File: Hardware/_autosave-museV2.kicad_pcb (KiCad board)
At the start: 2 copper layers, 288 parts, among them P1 RCA_conn_x2, P10 -15V, P11 ~3, P13 ~4, P14 +5V, P18 RX1, P19 3.3V, P2 +12V, P20 TX2, P21 1.8V, P22 PSU_CTL, P23 GND, P27 D1, P29 D2, P3 3.5mm_conn_tip_switch, P30 D3, P31 P1, P32 L1.8_1, P33 L3.3_1, P34 P2, P35 L1.8_2, P36 L3.3_2, P37 P3, P38 L1.8_3, P39 L3.3_3, P4 3.5mm_conn_tip_switch, P40 P4, P41 L1.8_4, P42 L3.3_4, P43 +5V, P44 +12V_AUX, P45 +5V_AUX, P5 CONN_01X06, P6 CONN_02X14, P7 ~5, P8 +15V, P9 ~6, Q1 PMOS, Q2 BSS138, SW1 PWR_BTN, SW2 PWR_BTN, U1 TPS65130, U10 PCM1863, U11 PCM1796, U12 NE5534, U13 NE5534, U14 NE5534, U15 NE5534, U16 NE5534, U17 NE5534, U18 EdisonConnector, U19 GTL2010, U2 LP38692, U20 GTL2010, U21 GTL2010, U22 PCA9685BS, U3 PLR135/T10, U4 POM-3535L-3-R, U5 POM-3535L-3-R, U6 PLT133/T10W, U7 POM-3535L-3-R, U8 POM-3535L-3-R, U9 PCM9211, X1 24.576 MHz

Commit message: PCB Layout progress - placing PCM9211 components
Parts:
- moved C18 165.2 mm to (184.2, 170.1), turned to 0 degrees
- moved C17 135.9 mm to (185.3, 171.8), turned to 0 degrees
- moved U11 13.4 mm to (166.2, 166.7)
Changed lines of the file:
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@@
   )
   (module Capacitors_SMD:C_0402 (layer F.Cu)
-    (at 29.217212 112.79591 180)
+    (at 184.2 170.05)
     (descr "Capacitor SMD 0402, reflow soldering, AVX (see smccp.pdf)")
     (tags "capacitor 0402")
     (attr smd)
-    (fp_text reference C18 (at 0 -1.7 180) (layer F.SilkS)
+    (fp_text reference C18 (at 0 -1.7) (layer F.SilkS) hide
       (effects (font (size 1 1) (thickness 0.15)))
     )
-    (fp_text value 0.1uF (at 0 1.7 180) (layer F.Fab)
+    (fp_text value 0.1uF (at 0 1.7) (layer F.Fab)
       (effects (font (size 1 1) (thickness 0.15)))
     )
@@
     (fp_line (start 0.25 -0.475) (end -0.25 -0.475) (layer F.SilkS) (width 0.15))
     (fp_line (start -0.25 0.475) (end 0.25 0.475) (layer F.SilkS) (width 0.15))
-    (pad 1 smd rect (at -0.55 0 180) (size 0.6 0.5) (layers F.Cu F.Paste F.Mask)
+    (pad 1 smd rect (at -0.55 0) (size 0.6 0.5) (layers F.Cu F.Paste F.Mask)
       (net 12 +3.3VSB))
-    (pad 2 smd rect (at 0.55 0 180) (size 0.6 0.5) (layers F.Cu F.Paste F.Mask)
+    (pad 2 smd rect (at 0.55 0) (size 0.6 0.5) (layers F.Cu F.Paste F.Mask)
       (net 2 GND))
     (model Capacitors_SMD.3dshapes/C_0402.wrl
@@
   )
   (module Housings_SSOP:SSOP-28_5.3x10.2mm_Pitch0.65mm (layer F.Cu)
-    (at 163.4 153.5 180)
+    (at 166.15 166.65 180)
     (descr "28-Lead Plastic Shrink Small Outline (SS)-5.30 mm Body [SSOP] (see Microchip Packaging Specification 00000049BS.pdf)")
     (tags "SSOP 0.65")
@@
   )
   (module Capacitors_SMD:C_1206 (layer F.Cu)
-    (at 58.473639 122.97091 180)
+    (at 185.3 171.8)
     (descr "Capacitor SMD 1206, reflow soldering, AVX (see smccp.pdf)")
     (tags "capacitor 1206")
     (attr smd)
-    (fp_text reference C17 (at 0 -2.3 180) (layer F.SilkS)
+    (fp_text reference C17 (at 0 -2.3) (layer F.SilkS) hide
       (effects (font (size 1 1) (thickness 0.15)))
     )
-    (fp_text value 10uF (at 0 2.3 180) (layer F.Fab)
+    (fp_text value 10uF (at 0 2.3) (layer F.Fab)
       (effects (font (size 1 1) (thickness 0.15)))
     )
@@
     (fp_line (start 1 -1.025) (end -1 -1.025) (layer F.SilkS) (width 0.15))
     (fp_line (start -1 1.025) (end 1 1.025) (layer F.SilkS) (width 0.15))
-    (pad 1 smd rect (at -1.5 0 180) (size 1 1.6) (layers F.Cu F.Paste F.Mask)
+    (pad 1 smd rect (at -1.5 0) (size 1 1.6) (layers F.Cu F.Paste F.Mask)
       (net 12 +3.3VSB))
-    (pad 2 smd rect (at 1.5 0 180) (size 1 1.6) (layers F.Cu F.Paste F.Mask)
+    (pad 2 smd rect (at 1.5 0) (size 1 1.6) (layers F.Cu F.Paste F.Mask)
       (net 2 GND))
     (model Capacitors_SMD.3dshapes/C_1206.wrl

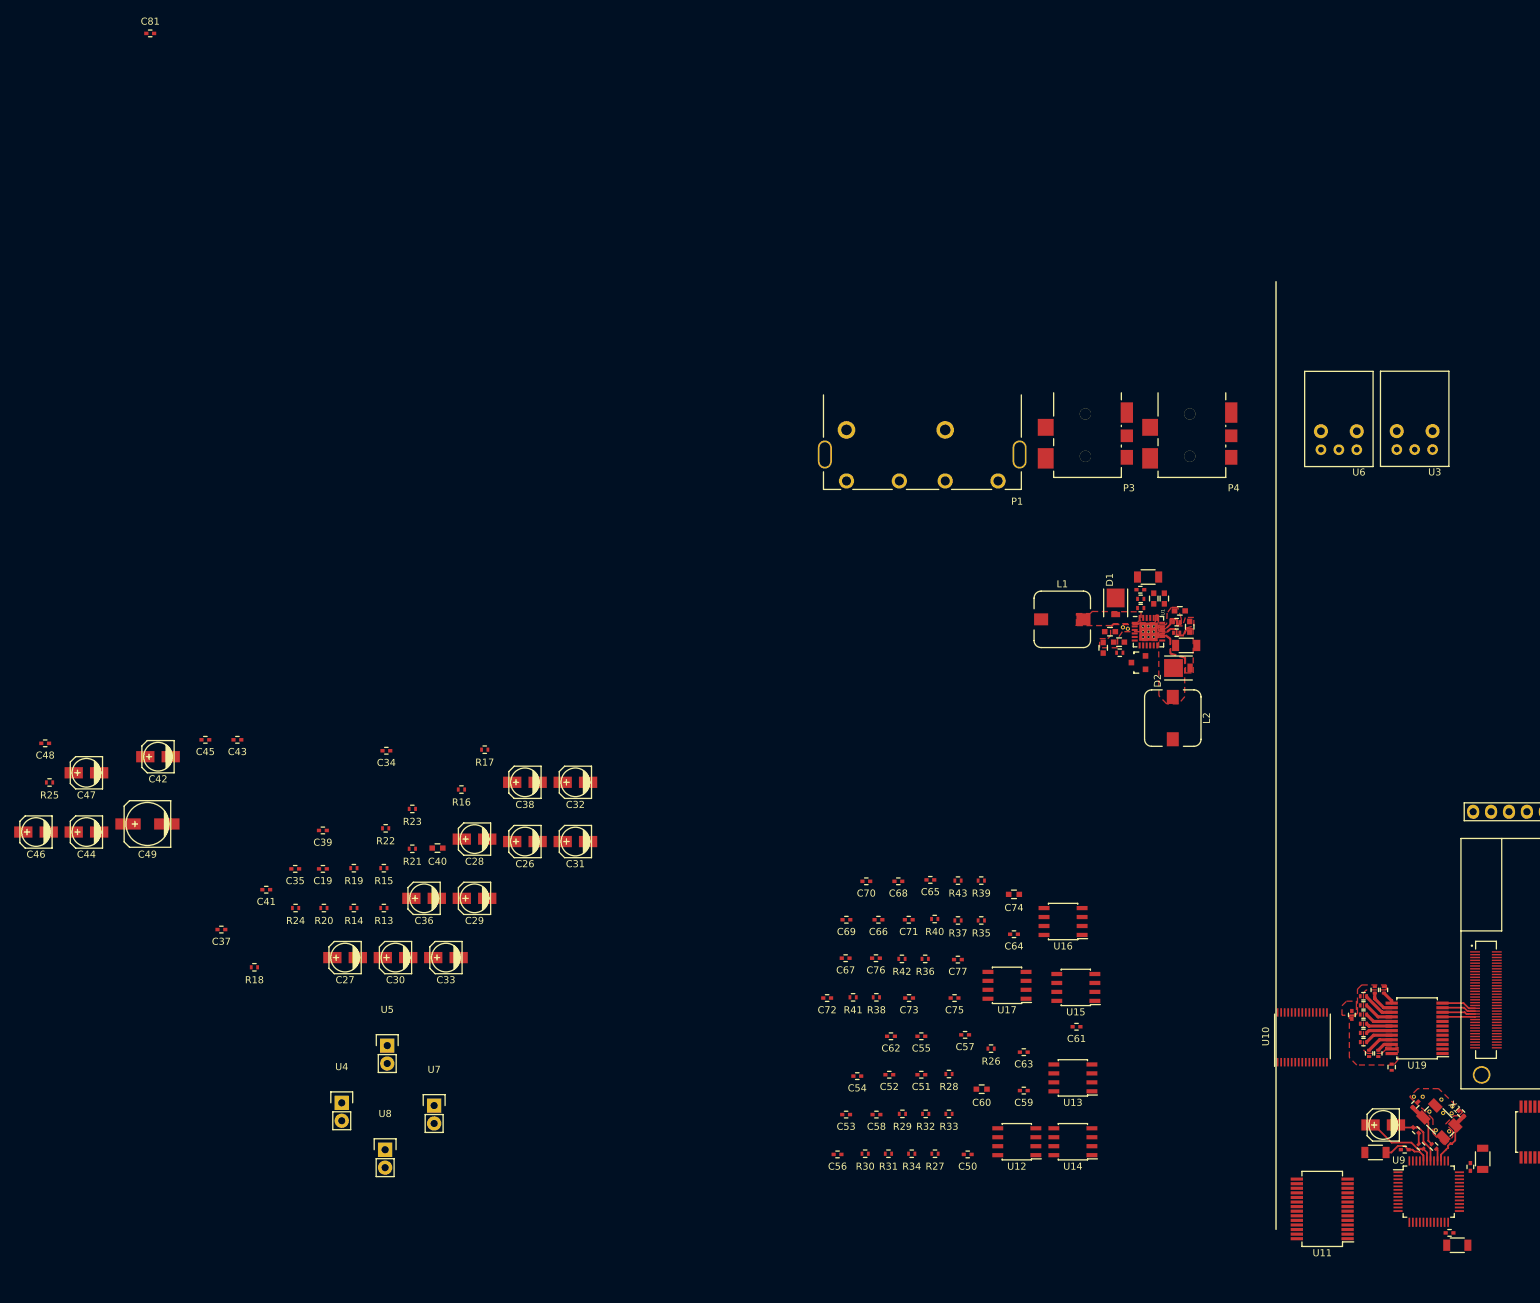
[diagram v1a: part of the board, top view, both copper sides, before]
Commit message: Placing ADC connections
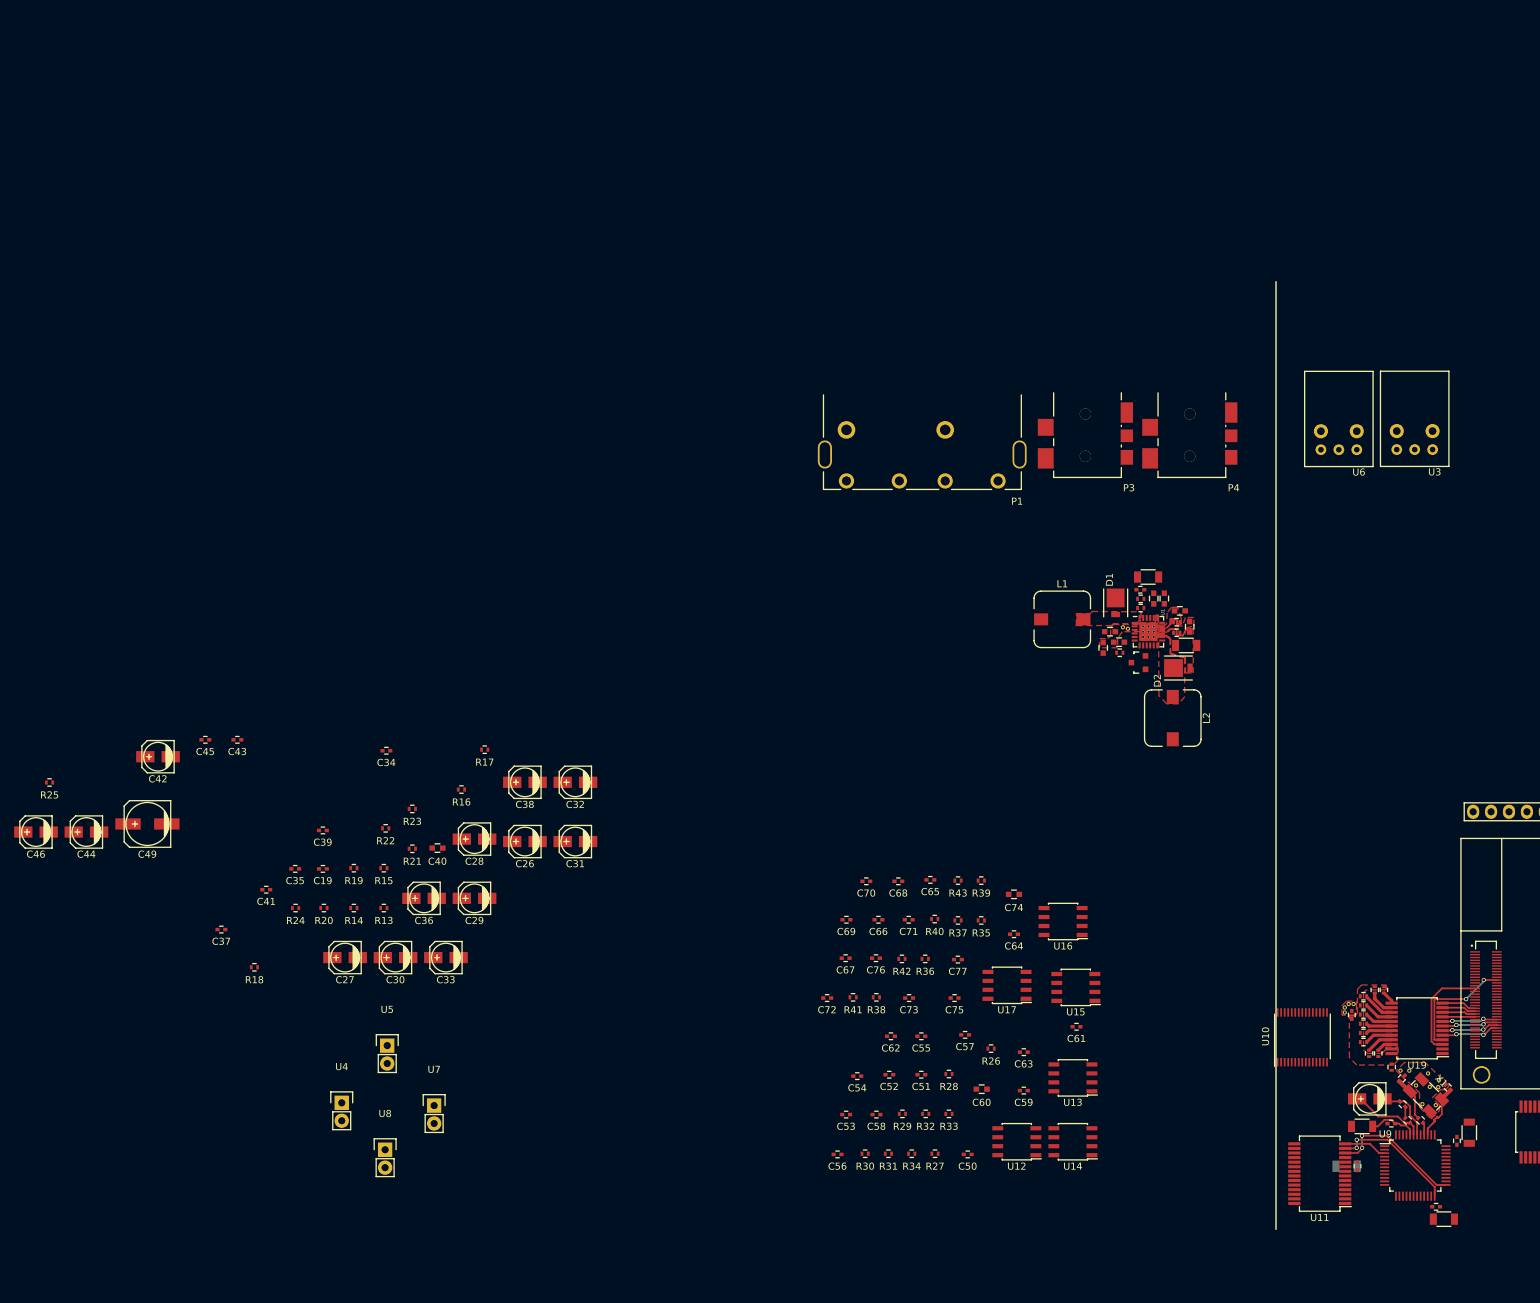
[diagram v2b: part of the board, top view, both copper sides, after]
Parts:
- removed C81: 10uF, Capacitors_SMD:C_0402
- added REF**: VIA-0.3mm, muse-v2-lib:VIA-0.3mm, F.Cu at (170.6, 137.6)
- added REF**: VIA-0.3mm, muse-v2-lib:VIA-0.3mm, F.Cu at (169.3, 138.8)
- added REF**: VIA-0.3mm, muse-v2-lib:VIA-0.3mm, F.Cu at (169.9, 137.6)
- added REF**: VIA-0.3mm, muse-v2-lib:VIA-0.3mm, F.Cu at (169.3, 138.1)
- C47: footprint Capacitors_SMD:c_elec_4x4.5 -> Capacitors_SMD:C_1206; moved to B.Cu
- moved C48 195.5 mm to (171.2, 160.6), turned to 270 degrees
- moved C47 187.2 mm to (169.6, 160.6)
- moved U11 5.01 mm to (165.8, 161.7)
- moved C15 4.16 mm to (187.0, 155.8)
- moved C17 4.16 mm to (183.4, 168.1)
- moved R12 4.16 mm to (178.2, 154.1)
- moved R6 4.16 mm to (180.1, 154.1)
- moved REF** 4.16 mm to (181.4, 149.3)
- moved REF** 4.16 mm to (182.2, 151.9)
- moved REF** 4.16 mm to (181.2, 147.4)
- moved C18 4.16 mm to (182.3, 166.3)
- moved C22 4.16 mm to (171.8, 154.9)
- moved C16 4.16 mm to (185.2, 157.0)
- moved C20 4.16 mm to (183.9, 149.4)
- moved C21 4.16 mm to (175.9, 154.6)
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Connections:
- C42 pad 1: +5VSB -> +5V
- C43 pad 1: +5VSB -> +5V
- C44 pad 1: +5VSB -> +5V
- C45 pad 1: +5VSB -> +5V
- C46 pad 1: +5VSB -> +5V
- C49 pad 1: +5VSB -> +5V
- P11 pad 1: (no net) -> MCU_GPIO_X_3/PWM_X_3
- P13 pad 1: (no net) -> MCU_GPIO_X_4/PWM_X_4
- P45 pad 1: (no net) -> +5V
- P5 pad 3: (no net) -> Net-(P5-Pad3)
- P5 pad 6: (no net) -> Net-(P5-Pad6)
- P6 pad 5: (no net) -> /LIGHT_CONN/LED_B_1
- P7 pad 1: (no net) -> MCU_GPIO_X_5/PWM_X_1
- P9 pad 1: (no net) -> MCU_GPIO_X_6/PWM_X_2
- U1 pad 12: (no net) -> Net-(U1-Pad12)
- U1 pad 20: (no net) -> Net-(U1-Pad20)
- U1 pad 25: GND -> (no net)
- U10 pad 10: (no net) -> Net-(U10-Pad10)
- U10 pad 19: (no net) -> Net-(U10-Pad19)
- U10 pad 22: (no net) -> Net-(U10-Pad22)
- U10 pad 9: (no net) -> Net-(U10-Pad9)
- U11 pad 1: (no net) -> Net-(U11-Pad1)
- U11 pad 15: +5VSB -> +5V
- U11 pad 2: (no net) -> Net-(U11-Pad2)
- U11 pad 23: +5VSB -> +5V
- U11 pad 28: +5VSB -> +5V
- U18 pad 10: (no net) -> Net-(U18-Pad10)
- U18 pad 16: (no net) -> Net-(U18-Pad16)
- U18 pad 18: (no net) -> Net-(U18-Pad18)
- U18 pad 19: (no net) -> Net-(U18-Pad19)
- U18 pad 20: (no net) -> Net-(U18-Pad20)
- U18 pad 21: (no net) -> Net-(U18-Pad21)
- U18 pad 23: (no net) -> Net-(U18-Pad23)
- U18 pad 24: (no net) -> Net-(U18-Pad24)
- U18 pad 3: (no net) -> Net-(U18-Pad3)
- U18 pad 31: (no net) -> Net-(U18-Pad31)
- U18 pad 33: (no net) -> MCU_GPIO_X_4/PWM_X_2
- U18 pad 35: (no net) -> MCU_GPIO_X_3/PWM_X_1
- U18 pad 37: (no net) -> MCU_GPIO_X_5/PWM_X_3
- U18 pad 39: (no net) -> MCU_GPIO_X_6/PWM_X_4
- U18 pad 67: (no net) -> Net-(U18-Pad67)
- U18 pad 69: (no net) -> Net-(U18-Pad69)
- U18 pad 7: (no net) -> Net-(U18-Pad7)
- U18 pad 8: (no net) -> Net-(U18-Pad8)
- U9 pad 1: (no net) -> Net-(U9-Pad1)
- U9 pad 16: (no net) -> Net-(U9-Pad16)
- U9 pad 2: (no net) -> Net-(U9-Pad2)
- U9 pad 32: (no net) -> Net-(U9-Pad32)
- U9 pad 35: (no net) -> Net-(U9-Pad35)
- U9 pad 37: (no net) -> Net-(U9-Pad37)
- U9 pad 47: (no net) -> Net-(U9-Pad47)
- U9 pad 48: (no net) -> Net-(U9-Pad48)
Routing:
- net I2C_SCL(3.3): track 1.88 -> 21.2 mm, vias 0 -> 2
- net I2C_SDA(3.3): track 0.00 -> 18.0 mm, vias 0 -> 2
- net UART_RX(1.8): track 0.00 -> 16.9 mm, vias 0 -> 2
- net UART_TX(1.8): track 0.00 -> 14.6 mm
- net I2S_MCU_DOUT(1.8): track 0.00 -> 8.21 mm, vias 0 -> 2
- net I2S_MCU_LRCK(1.8): track 0.00 -> 8.02 mm, vias 0 -> 2
- net I2S_MCU_BCK(1.8): track 0.00 -> 7.91 mm, vias 0 -> 2
- net I2S_MCU_DIN(1.8): track 0.00 -> 7.90 mm, vias 0 -> 2
- net DAC_RST: track 0.00 -> 6.15 mm
